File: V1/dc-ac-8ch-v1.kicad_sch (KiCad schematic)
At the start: 102 parts, among them J1 DB142V-5.08-4P, J2 DB142V-5.08-4P, J3 DB142V-5.08-2P, J4 DB142V-5.08-4P, J5 DB142V-5.08-4P, J6 DB142V-5.08-2P, U1 MOC3063S, U2 MOC3063S, U3 MOC3063S, U4 MOC3063S, U5 MOC3063S, U6 MOC3063S, U7 MOC3063S, U8 MOC3063S

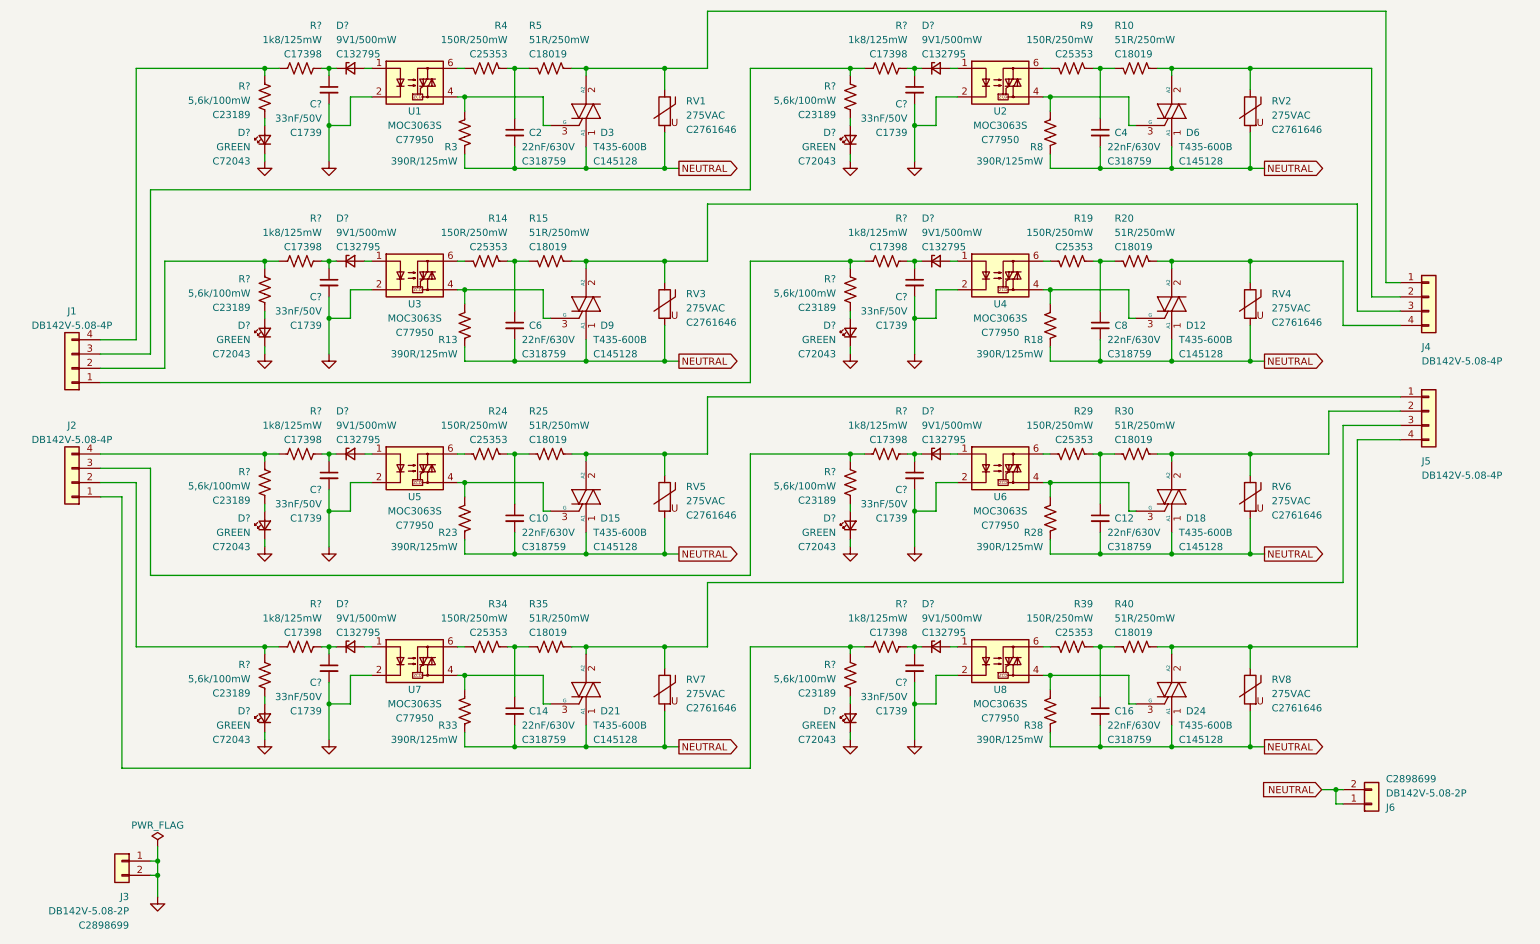
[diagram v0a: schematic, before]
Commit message: Place missing track under zone
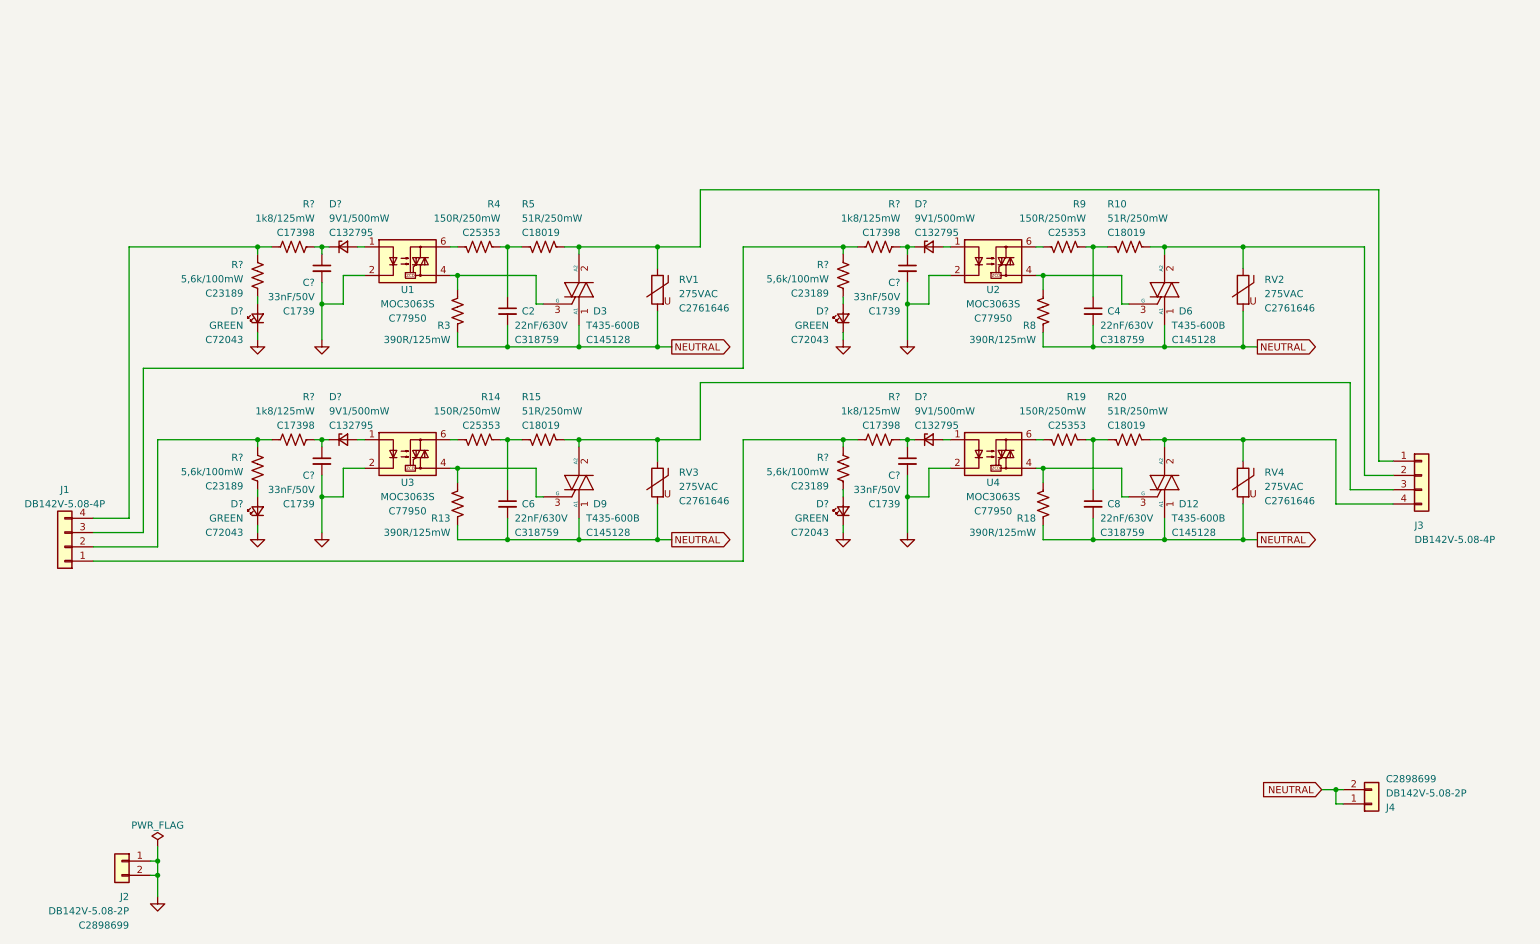
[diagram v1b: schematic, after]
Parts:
- removed C10, C12, C14, C16: 22nF/630V, Tales:C_1206_3216Metric, symbol Device:C_Small
- removed C? (x4): 33nF/50V, Tales:C_0805_2012Metric, symbol Device:C_Small
- removed D15, D18, D21, D24: T435-600B, Tales:TO-252-2, symbol Tales:T435-600B
- removed D? (x4): GREEN, Tales:LED_0603_1608Metric, symbol Device:LED_Small
- removed D? (x4): 9V1/500mW, Tales:D_SOD-123, symbol Device:D_Zener_Small
- removed J2, J5: DB142V-5.08-4P, Tales:TerminalBlock_Dibo_DB142V-5.08-4P_1x04_P5.08mm_Vertical, symbol Connector_Generic:Conn_01x04
- removed R23, R28, R33, R38: 390R/125mW, Tales:R_0805_2012Metric, symbol Device:R_US
- removed R24, R29, R34, R39: 150R/250mW, Tales:R_1206_3216Metric, symbol Device:R_US
- removed R25, R30, R35, R40: 51R/250mW, Tales:R_1206_3216Metric, symbol Device:R_US
- removed R? (x4): 1k8/125mW, Tales:R_0805_2012Metric, symbol Device:R_US
- removed R? (x4): 5,6k/100mW, Tales:R_0603_1608Metric, symbol Device:R_US
- removed RV5, RV6, RV7, RV8: 275VAC, Tales:RV_Disc_D9.50mm_W3.6mm_P5.08mm, symbol Device:Varistor
- removed U5, U6, U7, U8: MOC3063S, Tales:SMDIP-6_W9.53mm_Clearance8mm, symbol Relay_SolidState:MOC3063M
- renumbered J3 to J2, J4 to J3, J6 to J4
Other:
- moved on the sheet: C2, C4, C6, C8, C?, D12, D3, D6, D9, D?, J1, J3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
